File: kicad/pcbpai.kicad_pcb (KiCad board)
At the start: 2 copper layers, 68 x 98 mm, 24 parts, among them J1 Fuse, J10 Conn_01x02_Socket, J11 Conn_01x02_Socket, J12 Conn_01x02_Socket, J2 Conn_01x08_Socket, J3 Input 24 V, J4 Boton Encendido, J5 Parada de Emergencia, J6 Conn_01x08_Socket, J7 Raspberry GPIO, J8 Conn_01x02_Socket, J9 Conn_01x02_Socket, M1 MountingHole_2.5mm_Pad, M2 MountingHole_2.5mm_Pad, M3 MountingHole_2.5mm_Pad, M4 MountingHole_2.5mm_Pad, U6 ATtiny85-20P

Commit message: add gerber files and change footprints
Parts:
- D1, D2, D3, D4: footprint Connector_PinHeader_2.54mm:PinHeader_2x04_P2.54mm_Vertical -> Connector_IDC:IDC-Header_2x05_P2.54mm_Vertical
- J7: footprint Connector_PinHeader_2.54mm:PinHeader_2x20_P2.54mm_Vertical -> Connector_IDC:IDC-Header_2x20_P2.54mm_Vertical
- moved D3 6.43 mm to (130.1, 101.1)
- moved J12 4.90 mm to (120.9, 93.4)
- moved J6 4.15 mm to (151.6, 102.8)
- moved J10 4.11 mm to (167.5, 97.6)
- moved U6 4.00 mm to (160.8, 72.0)
- moved D1 3.70 mm to (158.1, 90.5)
- moved J2 3.35 mm to (136.5, 120.3)
- moved D4 1.90 mm to (130.4, 131.4)
- moved D2 1.90 mm to (158.2, 121.3)
- moved J11 1.53 mm to (120.5, 123.3)
- moved J8 0.44 mm to (167.4, 129.1)
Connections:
- D1 pad 1: +3.3V -> Net-(D1-RPWM)
- D1 pad 2: GND -> Net-(D1-LPWM)
- D1 pad 3: unconnected-(D1-Pad3) -> Net-(D1-L_EN)
- D1 pad 4: unconnected-(D1-Pad4) -> Net-(D1-L_EN)
- D1 pad 5: Net-(D1-EL) -> unconnected-(D1-R_IS-Pad5)
- D1 pad 6: Net-(D1-EL) -> unconnected-(D1-L_IS-Pad6)
- D1 pad 7: Net-(D1-PWMR) -> +3.3V
- D1 pad 8: Net-(D1-PWML) -> GND
- D2 pad 1: +3.3V -> Net-(D2-RPWM)
- D2 pad 2: GND -> Net-(D2-LPWM)
- D2 pad 3: unconnected-(D2-Pad3) -> Net-(D2-L_EN)
- D2 pad 4: unconnected-(D2-Pad4) -> Net-(D2-L_EN)
- D2 pad 5: Net-(D2-EL) -> unconnected-(D2-R_IS-Pad5)
- D2 pad 6: Net-(D2-EL) -> unconnected-(D2-L_IS-Pad6)
- D2 pad 7: Net-(D2-PWMR) -> +3.3V
- D2 pad 8: Net-(D2-PWML) -> GND
- D3 pad 1: +3.3V -> Net-(D3-RPWM)
- D3 pad 2: GND -> Net-(D3-LPWM)
- D3 pad 3: unconnected-(D3-Pad3) -> Net-(D3-L_EN)
- D3 pad 4: unconnected-(D3-Pad4) -> Net-(D3-L_EN)
- D3 pad 5: Net-(D3-EL) -> unconnected-(D3-R_IS-Pad5)
- D3 pad 6: Net-(D3-EL) -> unconnected-(D3-L_IS-Pad6)
- D3 pad 7: Net-(D3-PWMR) -> +3.3V
- D3 pad 8: Net-(D3-PWML) -> GND
- D4 pad 1: +3.3V -> Net-(D4-RPWM)
- D4 pad 2: GND -> Net-(D4-LPWM)
- D4 pad 3: unconnected-(D4-Pad3) -> Net-(D4-L_EN)
- D4 pad 4: unconnected-(D4-Pad4) -> Net-(D4-L_EN)
- D4 pad 5: Net-(D4-EL) -> unconnected-(D4-R_IS-Pad5)
- D4 pad 6: Net-(D4-EL) -> unconnected-(D4-L_IS-Pad6)
- D4 pad 7: Net-(D4-PWMR) -> +3.3V
- D4 pad 8: Net-(D4-PWML) -> GND
- J7 pad 11: Net-(D3-EL) -> Net-(D3-L_EN)
- J7 pad 12: Net-(D1-EL) -> Net-(D1-L_EN)
- J7 pad 13: Net-(D3-PWMR) -> Net-(D3-RPWM)
- J7 pad 15: Net-(D3-PWML) -> Net-(D3-LPWM)
- J7 pad 16: Net-(D1-PWMR) -> Net-(D1-RPWM)
- J7 pad 18: Net-(D1-PWML) -> Net-(D1-LPWM)
- J7 pad 33: Net-(D4-EL) -> Net-(D4-L_EN)
- J7 pad 35: Net-(D4-PWMR) -> Net-(D4-RPWM)
- J7 pad 36: Net-(D2-EL) -> Net-(D2-L_EN)
- J7 pad 37: Net-(D4-PWML) -> Net-(D4-LPWM)
- J7 pad 38: Net-(D2-PWMR) -> Net-(D2-RPWM)
- J7 pad 40: Net-(D2-PWML) -> Net-(D2-LPWM)
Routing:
- net Net-(D3-PWML): track 29.1 -> 0.00 mm
- net Net-(D4-EL): track 26.4 -> 0.00 mm
- net Net-(D3-EL): track 26.3 -> 0.00 mm
- net Net-(D1-LPWM): track 0.00 -> 25.5 mm
- net Net-(D2-LPWM): track 0.00 -> 23.8 mm
- net Net-(D2-L_EN): track 0.00 -> 23.5 mm
- net Net-(D1-RPWM): track 0.00 -> 22.8 mm
- net Net-(D3-LPWM): track 0.00 -> 22.7 mm
- net Net-(D1-PWML): track 21.8 -> 0.00 mm
- net Net-(D4-PWML): track 20.1 -> 0.00 mm
- net Net-(D3-PWMR): track 20.0 -> 0.00 mm
- net Net-(D1-EL): track 18.5 -> 0.00 mm
- net Net-(D4-RPWM): track 0.00 -> 17.9 mm
- net Net-(D2-PWML): track 17.5 -> 0.00 mm
- net Net-(D1-L_EN): track 0.00 -> 17.1 mm
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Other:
- board text added: "Camilo Barrera Camilo Borda Cristian Chitiva Johan Díaz Sebastian Dueñas Fernando Mendieta Juan Pablo Vallejo"
- board text added: "PAI3B"
- board text added: "SIMA"

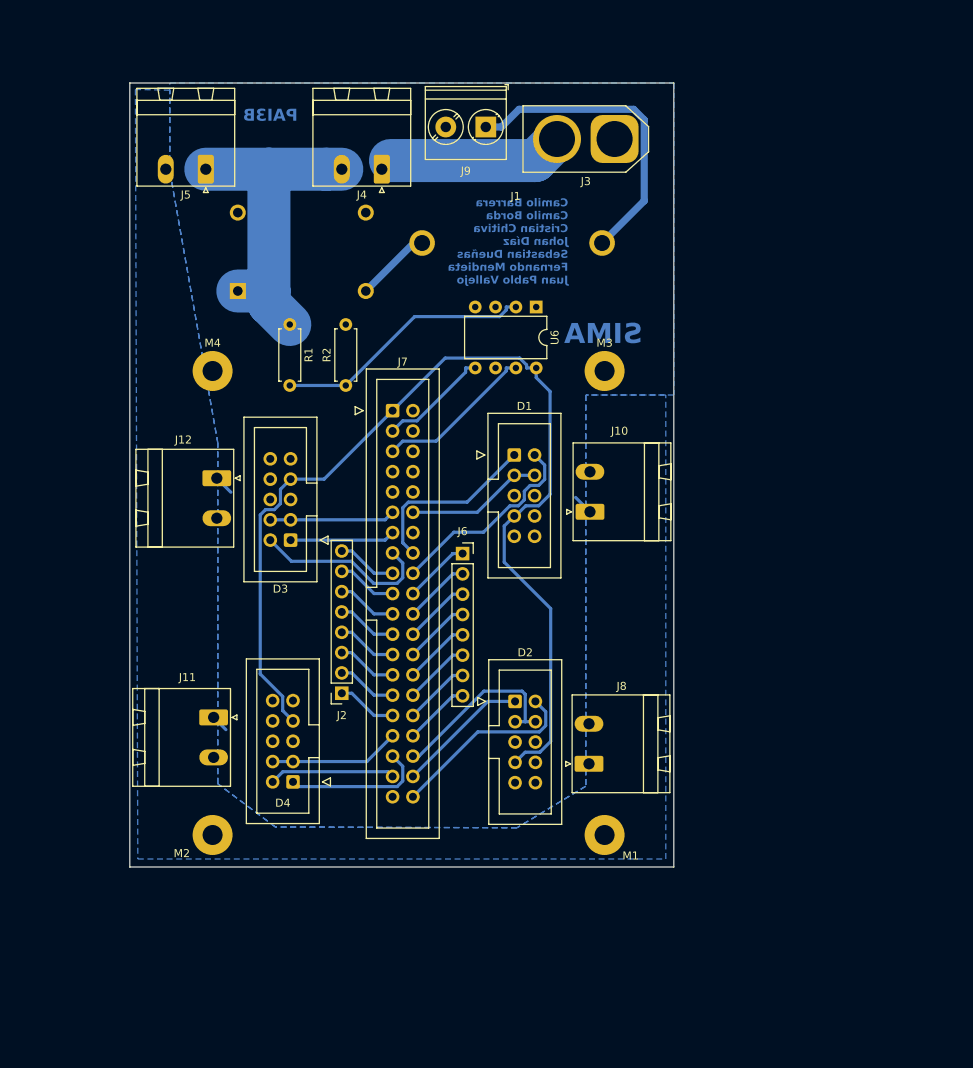
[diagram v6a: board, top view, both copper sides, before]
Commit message: fix xt60 polarity
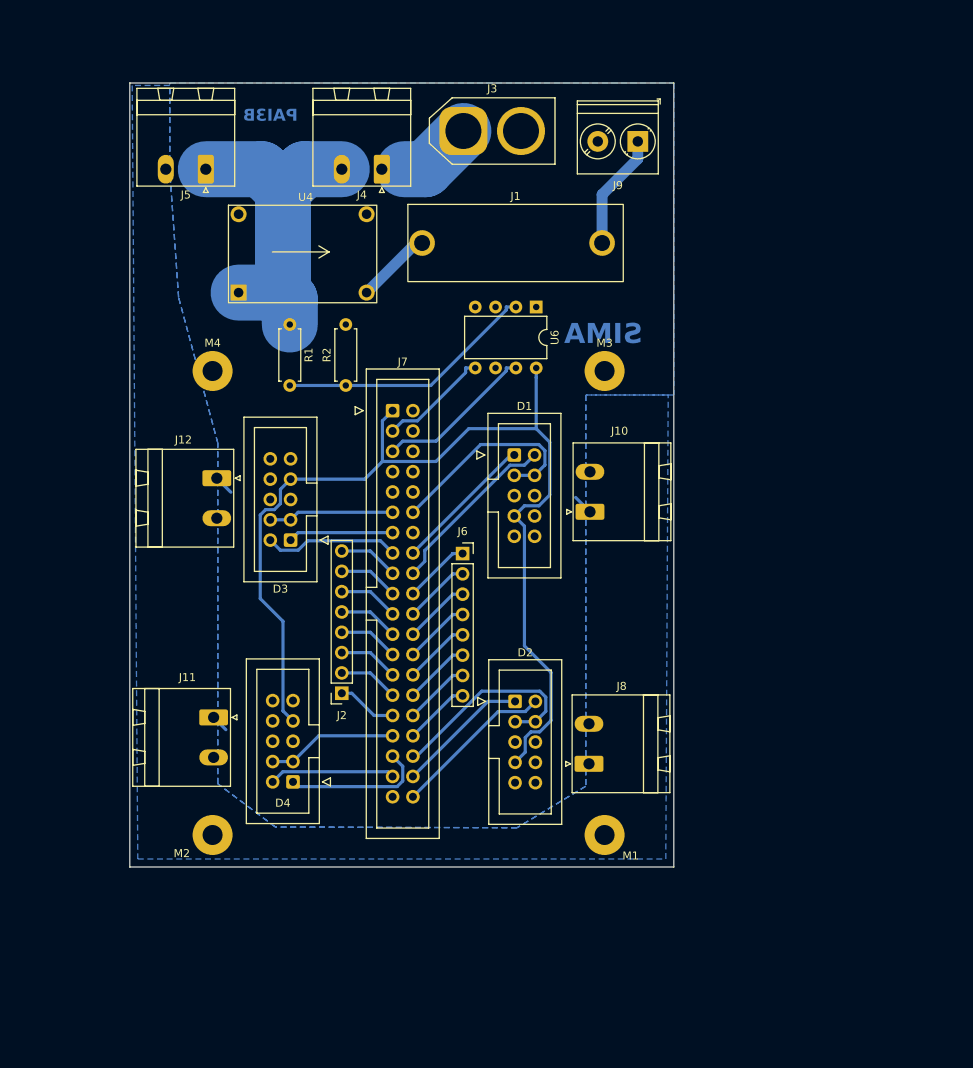
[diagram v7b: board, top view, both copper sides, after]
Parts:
- moved J9 19.1 mm to (173.5, 51.3)
- moved J3 18.9 mm to (151.7, 50.0), turned to 0 degrees
- moved U4 0.22 mm to (123.6, 70.2)
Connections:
- J3 pad 1: GND -> +24V
- J3 pad 2: +24V -> GND
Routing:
- net Net-(J1-Pin_2): track 38.8 -> 14.5 mm
- net +24V: track 23.5 -> 12.2 mm
- net Net-(D1-L_EN): track 17.1 -> 26.5 mm
- net Net-(D3-LPWM): track 22.7 -> 16.9 mm
- net Net-(D1-RPWM): track 22.8 -> 17.7 mm
- net Net-(D2-LPWM): track 23.8 -> 20.2 mm
- net Net-(D1-LPWM): track 25.5 -> 22.1 mm
- net Net-(D2-L_EN): track 23.5 -> 26.4 mm
- net +3.3V: track 130.6 -> 131.6 mm
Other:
- board text removed: "Camilo Barrera Camilo Borda Cristian Chitiva Johan Díaz Sebastian Dueñas Fernando Mendieta Juan Pablo Vallejo"
